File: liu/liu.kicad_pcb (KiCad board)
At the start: 2 copper layers, 101.6 x 66 mm, 16 parts, among them J1 Screw Termial, J2 Screw Terminal, J5 I2C, J6 RotaryEncoder, U1 VoltageRegulator, U2 ESP32, U3 TJA1050

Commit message: added stuff
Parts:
- added D2: D, Resistor_THT:R_Axial_DIN0207_L6.3mm_D2.5mm_P10.16mm_Horizontal, F.Cu at (78.7, 58.4)
- added R5: ~, Resistor_THT:R_Axial_DIN0207_L6.3mm_D2.5mm_P10.16mm_Horizontal, F.Cu at (81.3, 73.7)
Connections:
- U1 pad 4: /5V -> Net-(D2-A)
- U3 pad 2: Net-(U2-Pin_1) -> Net-(U3-Pin_2)
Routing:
- net Net-(U2-Pin_1): track 77.0 -> 61.8 mm
- net Net-(D2-A): track 0.00 -> 10.8 mm
- net /5V: track 148.9 -> 138.8 mm
- net Net-(U3-Pin_2): track 0.00 -> 5.08 mm

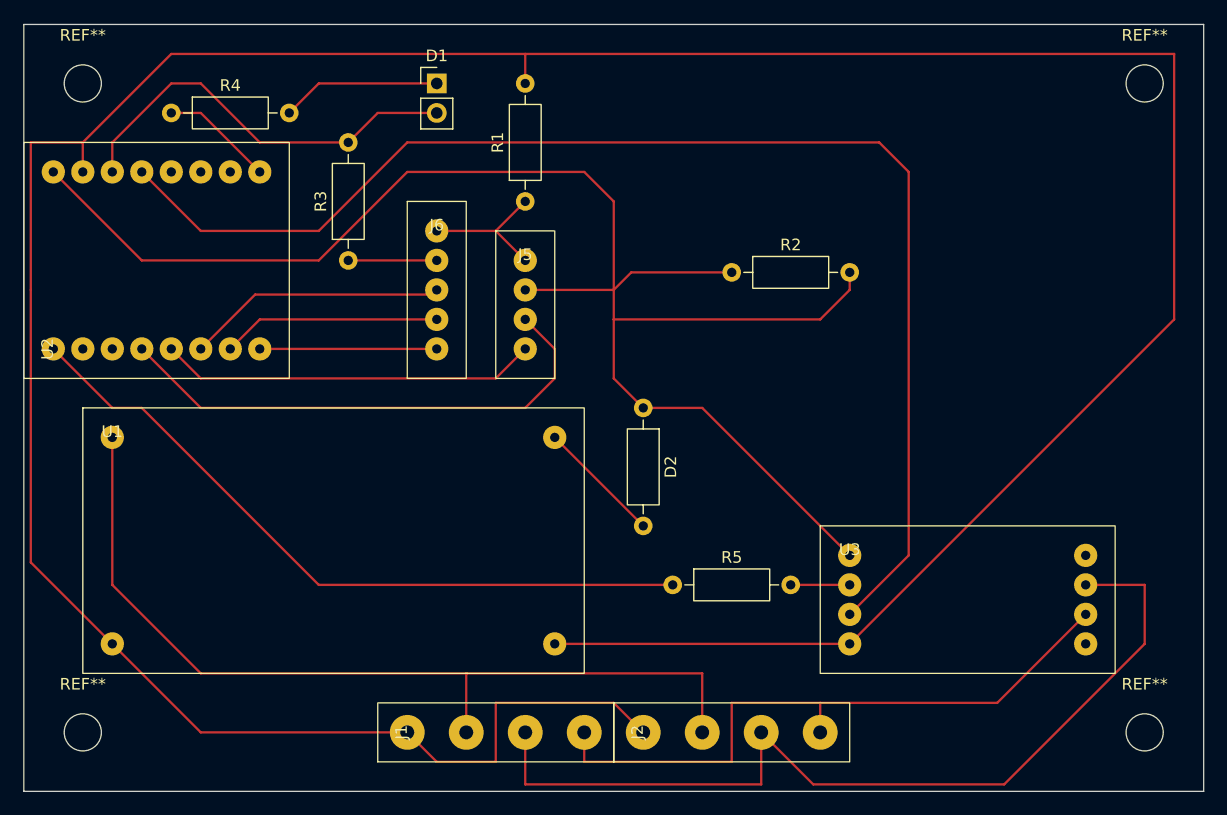
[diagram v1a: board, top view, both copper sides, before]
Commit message: merge front and back layer
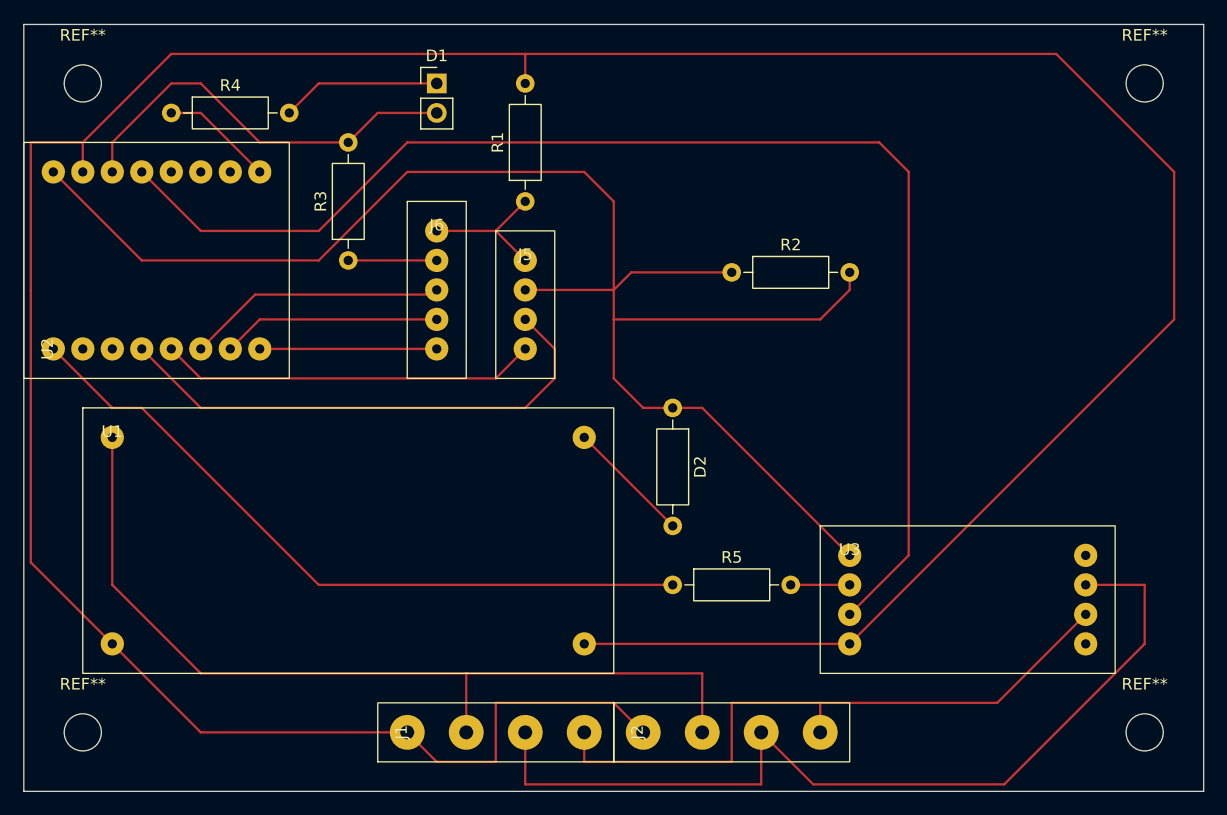
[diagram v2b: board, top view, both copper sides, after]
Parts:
- moved D2 2.54 mm to (81.3, 58.4)
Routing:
- net /GND: track 308.9 -> 250.5 mm
- net Net-(U2-Pin_1): track 61.8 -> 31.3 mm
- net Net-(D2-A): track 10.8 -> 0.00 mm
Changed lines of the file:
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@@
 	(footprint "Resistor_THT:R_Axial_DIN0207_L6.3mm_D2.5mm_P10.16mm_Horizontal"
 		(layer "F.Cu")
-		(at 78.74 58.42 -90)
+		(at 81.28 58.42 -90)
 		(descr "Resistor, Axial_DIN0207 series, Axial, Horizontal, pin pitch=10.16mm, 0.25W = 1/4W, length*diameter=6.3*2.5mm^2, http://cdn-reichelt.de/documents/datenblatt/B400/1_4W%23YAG.pdf")
 		(tags "Resistor Axial_DIN0207 series Axial Horizontal pin pitch 10.16mm 0.25W = 1/4W length 6.3mm diameter 2.5mm")
@@
 		(fp_rect
 			(start -2.54 -2.54)
-			(end 40.64 20.32)
+			(end 43.18 20.32)
 			(stroke
 				(width 0.1)
@@
 		)
 		(pad "3" thru_hole circle
-			(at 38.1 17.78)
+			(at 40.64 17.78)
 			(size 2 2)
 			(drill 0.8)
@@
 		)
 		(pad "4" thru_hole circle
-			(at 38.1 0)
+			(at 40.64 0)
 			(size 2 2)
 			(drill 0.8)
@@
 		(embedded_fonts no)
 	)
+	(gr_line
+		(start 73.66 60.96)
+		(end 81.28 68.58)
+		(stroke
+			(width 0.2)
+			(type default)
+		)
+		(layer "F.Cu")
+		(net 23)
+	)
+	(gr_line
+		(start 124.46 50.8)
+		(end 124.46 38.1)
+		(stroke
+			(width 0.2)
+			(type default)
+		)
+		(layer "F.Cu")
+		(net 4)
+	)
+	(gr_line
+		(start 114.3 27.94)
+		(end 124.46 38.1)
+		(stroke
+			(width 0.2)
+			(type default)
+		)
+		(layer "F.Cu")
+		(net 4)
+	)
+	(gr_line
+		(start 73.66 78.74)
+		(end 96.52 78.74)
+		(stroke
+			(width 0.2)
+			(type default)
+		)
+		(layer "F.Cu")
+		(net 4)
+	)
+	(gr_line
+		(start 50.8 73.66)
+		(end 81.28 73.66)
+		(stroke
+			(width 0.2)
+			(type default)
+		)
+		(layer "F.Cu")
+		(net 17)
+	)
 	(gr_rect
 		(start 25.4 25.4)
@@
 	)
 	(segment
-		(start 68.58 27.94)
-		(end 124.46 27.94)
-		(width 0.2)
-		(layer "F.Cu")
-		(net 4)
-	)
-	(segment
 		(start 68.58 30.48)
 		(end 68.58 27.94)
@@
 	)
 	(segment
-		(start 71.12 78.74)
-		(end 96.52 78.74)
+		(start 114.3 27.94)
+		(end 68.58 27.94)
 		(width 0.2)
 		(layer "F.Cu")
@@
 	)
 	(segment
-		(start 124.46 27.94)
-		(end 124.46 50.8)
-		(width 0.2)
-		(layer "F.Cu")
-		(net 4)
-	)
-	(segment
 		(start 60.96 88.9)
 		(end 66.04 88.9)
@@
 	)
 	(segment
-		(start 50.8 73.66)
-		(end 81.28 73.66)
-		(width 0.2)
-		(layer "F.Cu")
-		(net 17)
-	)
-	(segment
 		(start 27.94 53.34)
 		(end 33.02 58.42)
@@
 	)
 	(segment
-		(start 71.12 60.96)
-		(end 78.74 68.58)
-		(width 0.2)
-		(layer "F.Cu")
-		(net 23)
-	)
-	(segment
